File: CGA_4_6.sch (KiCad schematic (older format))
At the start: 11 parts, among them U1 74S112, U2 74LS74, U25 74LS00, U26 74S04, U28 74LS10, U29 74S04, U30 74LS32, U46 74LS00, U47 74LS51, U49 74LS02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

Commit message: More sheet 4
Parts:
- added U27: 74LS51, Package_DIP:DIP-14_W7.62mm_LongPads, symbol 74xx:74LS51
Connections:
- net HRES: now also U27.2
- net ~CCLK: now also U27.6
- net ~HRES: now also U27.4
- new net HCLK: U27.3
- new net LCLK: U27.5
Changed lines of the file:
@@
 Wire Wire Line
 	5500 2200 5800 2200
+$Comp
+L 74xx:74LS51 U27
+U 2 1 62FE2980
+P 2050 6650
+F 0 "U27" H 2050 7175 50  0000 C CNN
+F 1 "74LS51" H 2050 7084 50  0000 C CNN
+F 2 "Package_DIP:DIP-14_W7.62mm_LongPads" H 2050 6650 50  0001 C CNN
+F 3 "http://www.ti.com/lit/ds/symlink/sn74ls51.pdf" H 2050 6650 50  0001 C CNN
+	2    2050 6650
+	1    0    0    -1
+$EndComp
+$Comp
+L 74xx:74LS51 U27
+U 1 1 62FEE44E
+P 2050 7900
+F 0 "U27" H 2050 8425 50  0000 C CNN
+F 1 "74LS51" H 2050 8334 50  0000 C CNN
+F 2 "Package_DIP:DIP-14_W7.62mm_LongPads" H 2050 7900 50  0001 C CNN
+F 3 "http://www.ti.com/lit/ds/symlink/sn74ls51.pdf" H 2050 7900 50  0001 C CNN
+	1    2050 7900
+	1    0    0    -1
+$EndComp
+Wire Wire Line
+	1550 6350 1050 6350
+Text GLabel 1050 6350 0    50   Input ~ 0
+HRES
+Wire Wire Line
+	1550 6550 1050 6550
+Text GLabel 1050 6550 0    50   Input ~ 0
+HCLK
+Wire Wire Line
+	1550 6750 1050 6750
+Text GLabel 1050 6750 0    50   Input ~ 0
+~HRES
+Wire Wire Line
+	1550 6950 1050 6950
+Text GLabel 1050 6950 0    50   Input ~ 0
+LCLK
+Text GLabel 2750 6650 2    50   Output ~ 0
+~CCLK
+Wire Wire Line
+	2750 6650 2550 6650
 $EndSCHEMATC

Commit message: More sheet 4
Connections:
- net HRES: now also U27.9
- net VCC: now also U27.10, U27.13
- net ~HRES: now also U27.12
- net ~7_MHZ: now reaches U27.1
- net ~14_MHZ: now reaches U27.11
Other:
- moved on the sheet: U27A, U27B
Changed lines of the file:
@@
 L 74xx:74LS51 U27
 U 2 1 62FE2980
-P 2050 6650
-F 0 "U27" H 2050 7175 50  0000 C CNN
-F 1 "74LS51" H 2050 7084 50  0000 C CNN
-F 2 "Package_DIP:DIP-14_W7.62mm_LongPads" H 2050 6650 50  0001 C CNN
-F 3 "http://www.ti.com/lit/ds/symlink/sn74ls51.pdf" H 2050 6650 50  0001 C CNN
-	2    2050 6650
+P 2100 6200
+F 0 "U27" H 2100 6725 50  0000 C CNN
+F 1 "74LS51" H 2100 6634 50  0000 C CNN
+F 2 "Package_DIP:DIP-14_W7.62mm_LongPads" H 2100 6200 50  0001 C CNN
+F 3 "http://www.ti.com/lit/ds/symlink/sn74ls51.pdf" H 2100 6200 50  0001 C CNN
+	2    2100 6200
 	1    0    0    -1
 $EndComp
@@
 L 74xx:74LS51 U27
 U 1 1 62FEE44E
-P 2050 7900
-F 0 "U27" H 2050 8425 50  0000 C CNN
-F 1 "74LS51" H 2050 8334 50  0000 C CNN
-F 2 "Package_DIP:DIP-14_W7.62mm_LongPads" H 2050 7900 50  0001 C CNN
-F 3 "http://www.ti.com/lit/ds/symlink/sn74ls51.pdf" H 2050 7900 50  0001 C CNN
-	1    2050 7900
+P 2100 7250
+F 0 "U27" H 2100 6760 50  0000 C CNN
+F 1 "74LS51" H 2100 6851 50  0000 C CNN
+F 2 "Package_DIP:DIP-14_W7.62mm_LongPads" H 2100 7250 50  0001 C CNN
+F 3 "http://www.ti.com/lit/ds/symlink/sn74ls51.pdf" H 2100 7250 50  0001 C CNN
+	1    2100 7250
+	1    0    0    1
+$EndComp
+Wire Wire Line
+	1600 5900 1200 5900
+Text GLabel 1100 5900 0    50   Input ~ 0
+HRES
+Wire Wire Line
+	1600 6100 1100 6100
+Text GLabel 1100 6100 0    50   Input ~ 0
+HCLK
+Wire Wire Line
+	1600 6300 1450 6300
+Text GLabel 1100 6300 0    50   Input ~ 0
+~HRES
+Wire Wire Line
+	1600 6500 1100 6500
+Text GLabel 1100 6500 0    50   Input ~ 0
+LCLK
+Text GLabel 2800 6200 2    50   Output ~ 0
+~CCLK
+Wire Wire Line
+	2800 6200 2600 6200
+Wire Wire Line
+	1600 7150 1200 7150
+Wire Wire Line
+	1200 7150 1200 5900
+Connection ~ 1200 5900
+Wire Wire Line
+	1200 5900 1100 5900
+Text GLabel 1100 6950 0    50   Input ~ 0
+~14_MHZ
+Wire Wire Line
+	1100 6950 1600 6950
+Wire Wire Line
+	1600 7050 1350 7050
+Wire Wire Line
+	1350 7050 1350 7300
+Wire Wire Line
+	1350 7350 1600 7350
+$Comp
+L power:VCC #PWR?
+U 1 1 630E9E72
+P 1100 7200
+F 0 "#PWR?" H 1100 7050 50  0001 C CNN
+F 1 "VCC" H 950 7250 50  0000 C CNN
+F 2 "" H 1100 7200 50  0001 C CNN
+F 3 "" H 1100 7200 50  0001 C CNN
+	1    1100 7200
 	1    0    0    -1
 $EndComp
 Wire Wire Line
-	1550 6350 1050 6350
-Text GLabel 1050 6350 0    50   Input ~ 0
-HRES
+	1100 7200 1100 7300
 Wire Wire Line
-	1550 6550 1050 6550
-Text GLabel 1050 6550 0    50   Input ~ 0
-HCLK
+	1100 7300 1350 7300
+Connection ~ 1350 7300
 Wire Wire Line
-	1550 6750 1050 6750
-Text GLabel 1050 6750 0    50   Input ~ 0
-~HRES
+	1350 7300 1350 7350
 Wire Wire Line
-	1550 6950 1050 6950
-Text GLabel 1050 6950 0    50   Input ~ 0
-LCLK
-Text GLabel 2750 6650 2    50   Output ~ 0
-~CCLK
+	1600 7450 1450 7450
 Wire Wire Line
-	2750 6650 2550 6650
+	1450 7450 1450 6300
+Connection ~ 1450 6300
+Wire Wire Line
+	1450 6300 1100 6300
+Text GLabel 1100 7550 0    50   Input ~ 0
+~7_MHZ
+Wire Wire Line
+	1600 7550 1100 7550
 $EndSCHEMATC

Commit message: More sheet 4
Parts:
- added unit 5 of U26
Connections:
- net DOT_CLOCK: now reaches U27.8
- net DOT_CLOCK: now also U26.11
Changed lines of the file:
@@
 Wire Wire Line
 	1600 7550 1100 7550
+$Comp
+L 74xx:74LS04 U?
+U 5 1 63106999
+P 3300 7250
+AR Path="/60463C57/63106999" Ref="U?"  Part="2"
+AR Path="/60463CC5/63106999" Ref="U26"  Part="5"
+F 0 "U26" H 3250 6950 50  0000 C CNN
+F 1 "74S04" H 3250 7050 50  0000 C CNN
+F 2 "Package_DIP:DIP-14_W7.62mm_LongPads" H 3300 7250 50  0001 C CNN
+F 3 "http://www.ti.com/lit/gpn/sn74LS04" H 3300 7250 50  0001 C CNN
+	5    3300 7250
+	1    0    0    -1
+$EndComp
+Wire Wire Line
+	2600 7250 2700 7250
+Wire Wire Line
+	2700 7250 2700 7700
+Wire Wire Line
+	2700 7700 3150 7700
+Connection ~ 2700 7250
+Wire Wire Line
+	2700 7250 3000 7250
+Text GLabel 3150 7700 2    50   Output ~ 0
+DOT_CLOCK
 $EndSCHEMATC

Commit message: More sheet 4
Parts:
- added unit 4 of U25
- added unit 1 of U25
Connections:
- net at U26.10: now also U25.13
- new net: U25.1, U25.11
- new net: U25.12, U25.3
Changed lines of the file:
@@
 Text GLabel 3150 7700 2    50   Output ~ 0
 DOT_CLOCK
+$Comp
+L 74xx:74LS00 U25
+U 4 1 6312E8E0
+P 4350 6900
+F 0 "U25" H 4350 6600 50  0000 C CNN
+F 1 "74LS00" H 4350 6700 50  0000 C CNN
+F 2 "Package_DIP:DIP-14_W7.62mm_LongPads" H 4350 6900 50  0001 C CNN
+F 3 "http://www.ti.com/lit/gpn/sn74ls00" H 4350 6900 50  0001 C CNN
+	4    4350 6900
+	1    0    0    1
+$EndComp
+$Comp
+L 74xx:74LS00 U25
+U 1 1 631459CB
+P 4350 7550
+F 0 "U25" H 4350 7250 50  0000 C CNN
+F 1 "74LS00" H 4350 7350 50  0000 C CNN
+F 2 "Package_DIP:DIP-14_W7.62mm_LongPads" H 4350 7550 50  0001 C CNN
+F 3 "http://www.ti.com/lit/gpn/sn74ls00" H 4350 7550 50  0001 C CNN
+	1    4350 7550
+	1    0    0    -1
+$EndComp
+Wire Wire Line
+	3600 7250 3800 7250
+Wire Wire Line
+	3800 7250 3800 6800
+Wire Wire Line
+	3800 6800 4050 6800
+Wire Wire Line
+	4650 6900 5000 6900
+Wire Wire Line
+	5000 6900 5000 7200
+Wire Wire Line
+	5000 7200 3900 7200
+Wire Wire Line
+	3900 7200 3900 7450
+Wire Wire Line
+	3900 7450 4050 7450
+Wire Wire Line
+	4650 7550 4900 7550
+Wire Wire Line
+	4900 7550 4900 7100
+Wire Wire Line
+	4900 7100 3900 7100
+Wire Wire Line
+	3900 7100 3900 7000
+Wire Wire Line
+	3900 7000 4050 7000
 $EndSCHEMATC

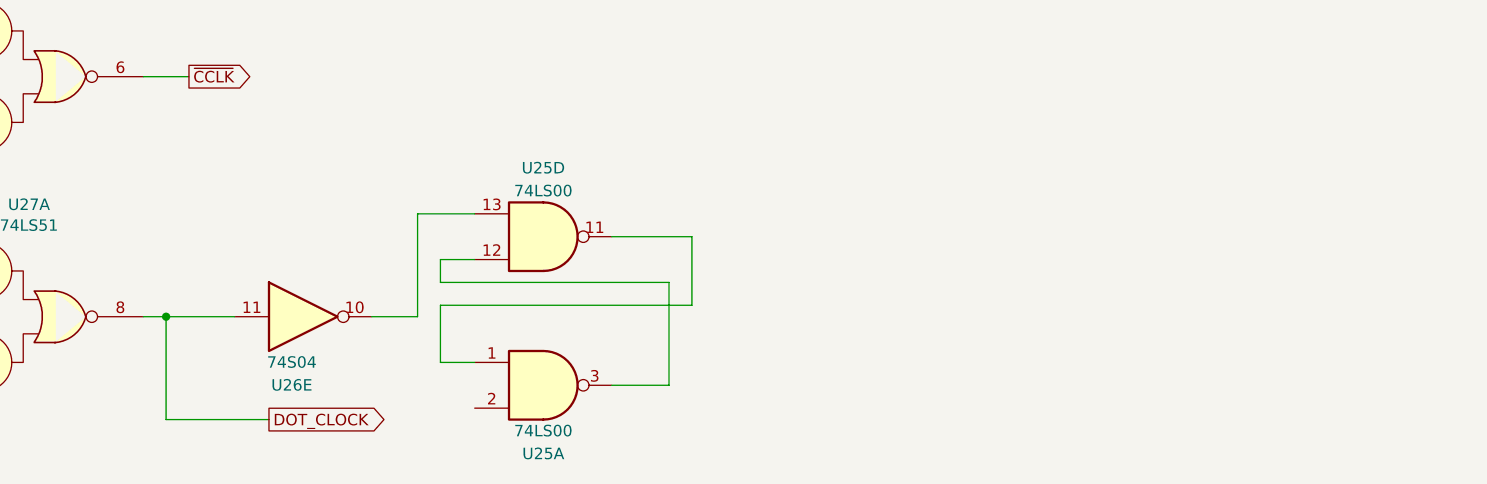
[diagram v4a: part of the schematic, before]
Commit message: Add more of sheet 4
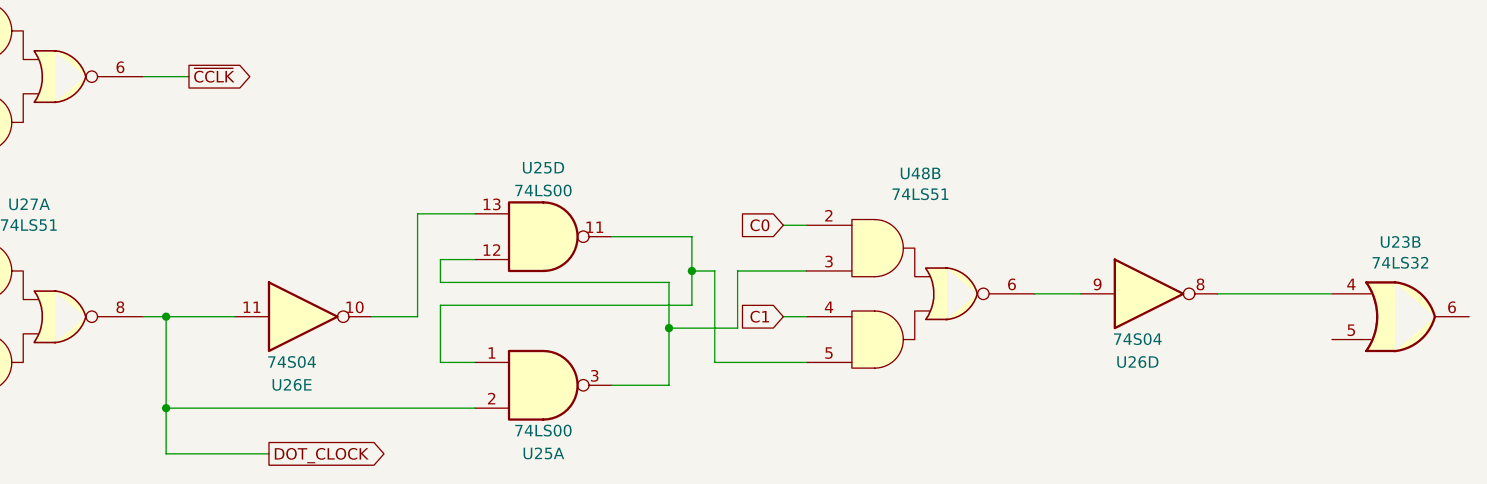
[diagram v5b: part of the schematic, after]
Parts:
- added U23: 74LS32, Package_DIP:DIP-14_W7.62mm_LongPads, symbol 74xx:74LS32
- added unit 4 of U26
- added U48: 74LS51, Package_DIP:DIP-14_W7.62mm_LongPads, symbol 74xx:74LS51
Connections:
- net DOT_CLOCK: now also U25.2
- net at U25.1, U25.11: now also U48.5
- net at U25.12, U25.3: now also U48.3
- new net: U26.9, U48.6
- new net: U23.4, U26.8
- new net C0: U48.2
- new net C1: U48.4
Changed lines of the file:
@@
 	2600 7250 2700 7250
 Wire Wire Line
-	2700 7250 2700 7700
-Wire Wire Line
-	2700 7700 3150 7700
+	2700 7850 3150 7850
 Connection ~ 2700 7250
 Wire Wire Line
 	2700 7250 3000 7250
-Text GLabel 3150 7700 2    50   Output ~ 0
+Text GLabel 3150 7850 2    50   Output ~ 0
 DOT_CLOCK
 $Comp
@@
 	4650 6900 5000 6900
 Wire Wire Line
-	5000 6900 5000 7200
+	5000 6900 5000 7050
 Wire Wire Line
 	5000 7200 3900 7200
@@
 	4650 7550 4900 7550
 Wire Wire Line
-	4900 7550 4900 7100
+	4900 7550 4900 7300
 Wire Wire Line
 	4900 7100 3900 7100
@@
 Wire Wire Line
 	3900 7000 4050 7000
+$Comp
+L 74xx:74LS51 U?
+U 2 1 63173D58
+P 6000 7150
+AR Path="/60463BAE/63173D58" Ref="U?"  Part="1"
+AR Path="/60463CC5/63173D58" Ref="U48"  Part="2"
+F 0 "U48" H 6000 7675 50  0000 C CNN
+F 1 "74LS51" H 6000 7584 50  0000 C CNN
+F 2 "Package_DIP:DIP-14_W7.62mm_LongPads" H 6000 7150 50  0001 C CNN
+F 3 "http://www.ti.com/lit/ds/symlink/sn74ls51.pdf" H 6000 7150 50  0001 C CNN
+	2    6000 7150
+	1    0    0    -1
+$EndComp
+Wire Wire Line
+	4900 7300 5200 7300
+Wire Wire Line
+	5200 7300 5200 7050
+Wire Wire Line
+	5200 7050 5500 7050
+Connection ~ 4900 7300
+Wire Wire Line
+	4900 7300 4900 7100
+Wire Wire Line
+	5000 7050 5100 7050
+Wire Wire Line
+	5100 7050 5100 7450
+Wire Wire Line
+	5100 7450 5500 7450
+Connection ~ 5000 7050
+Wire Wire Line
+	5000 7050 5000 7200
+Text GLabel 5400 7250 0    50   Input ~ 0
+C1
+Wire Wire Line
+	5400 7250 5500 7250
+Text GLabel 5400 6850 0    50   Input ~ 0
+C0
+Wire Wire Line
+	5400 6850 5500 6850
+$Comp
+L 74xx:74LS04 U?
+U 4 1 631E3E02
+P 7000 7150
+AR Path="/60463C57/631E3E02" Ref="U?"  Part="2"
+AR Path="/60463CC5/631E3E02" Ref="U26"  Part="4"
+F 0 "U26" H 6950 6850 50  0000 C CNN
+F 1 "74S04" H 6950 6950 50  0000 C CNN
+F 2 "Package_DIP:DIP-14_W7.62mm_LongPads" H 7000 7150 50  0001 C CNN
+F 3 "http://www.ti.com/lit/gpn/sn74LS04" H 7000 7150 50  0001 C CNN
+	4    7000 7150
+	1    0    0    -1
+$EndComp
+Wire Wire Line
+	6500 7150 6700 7150
+$Comp
+L 74xx:74LS32 U23
+U 2 1 631F965E
+P 8100 7250
+F 0 "U23" H 8100 7575 50  0000 C CNN
+F 1 "74LS32" H 8100 7484 50  0000 C CNN
+F 2 "Package_DIP:DIP-14_W7.62mm_LongPads" H 8100 7250 50  0001 C CNN
+F 3 "http://www.ti.com/lit/gpn/sn74LS32" H 8100 7250 50  0001 C CNN
+	2    8100 7250
+	1    0    0    -1
+$EndComp
+Wire Wire Line
+	7300 7150 7800 7150
+Wire Wire Line
+	2700 7250 2700 7650
+Wire Wire Line
+	4050 7650 2700 7650
+Connection ~ 2700 7650
+Wire Wire Line
+	2700 7650 2700 7850
 $EndSCHEMATC

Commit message: More sheet 4
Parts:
- added U15: 74LS00, Package_DIP:DIP-14_W7.62mm_LongPads, symbol 74xx:74LS00
- added unit 1 of U28
- added U65: 74LS02, Package_DIP:DIP-14_W7.62mm_LongPads, symbol 74xx:74LS02
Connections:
- net at U23.6: now also U28.13
- new net: U15.11, U28.1
- new net: U28.2, U65.4
- new net HSYNC_DLY: U65.6
- new net STR: U28.12
- new net VSYNC_DLY: U65.5
- new net ~DISPEN_DLY: U15.13
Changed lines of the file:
@@
 Wire Wire Line
 	2700 7650 2700 7850
+$Comp
+L 74xx:74LS00 U?
+U 4 1 63236E76
+P 8100 6600
+AR Path="/60463C57/63236E76" Ref="U?"  Part="4"
+AR Path="/60463CC5/63236E76" Ref="U15"  Part="4"
+F 0 "U15" H 8100 6283 50  0000 C CNN
+F 1 "74LS00" H 8100 6374 50  0000 C CNN
+F 2 "Package_DIP:DIP-14_W7.62mm_LongPads" H 8100 6600 50  0001 C CNN
+F 3 "http://www.ti.com/lit/gpn/sn74ls00" H 8100 6600 50  0001 C CNN
+	4    8100 6600
+	1    0    0    1
+$EndComp
+$Comp
+L 74xx:74LS02 U?
+U 2 1 6325627C
+P 8100 6000
+AR Path="/60463C57/6325627C" Ref="U?"  Part="4"
+AR Path="/60463CC5/6325627C" Ref="U65"  Part="2"
+F 0 "U65" H 8100 6325 50  0000 C CNN
+F 1 "74LS02" H 8100 6234 50  0000 C CNN
+F 2 "Package_DIP:DIP-14_W7.62mm_LongPads" H 8100 6000 50  0001 C CNN
+F 3 "http://www.ti.com/lit/gpn/sn74ls02" H 8100 6000 50  0001 C CNN
+	2    8100 6000
+	1    0    0    -1
+$EndComp
+$Comp
+L 74xx:74LS10 U?
+U 1 1 63279063
+P 9050 6700
+AR Path="/60463BAE/63279063" Ref="U?"  Part="3"
+AR Path="/60463CC5/63279063" Ref="U28"  Part="1"
+F 0 "U28" H 9050 7025 50  0000 C CNN
+F 1 "74LS10" H 9050 6934 50  0000 C CNN
+F 2 "Package_DIP:DIP-14_W7.62mm_LongPads" H 9050 6700 50  0001 C CNN
+F 3 "http://www.ti.com/lit/gpn/sn74LS10" H 9050 6700 50  0001 C CNN
+	1    9050 6700
+	1    0    0    -1
+$EndComp
+Wire Wire Line
+	8400 6600 8750 6600
+Wire Wire Line
+	8400 6000 8600 6000
+Wire Wire Line
+	8600 6000 8600 6700
+Wire Wire Line
+	8600 6700 8750 6700
+Wire Wire Line
+	8400 7250 8600 7250
+Wire Wire Line
+	8600 7250 8600 6800
+Wire Wire Line
+	8600 6800 8750 6800
+Text GLabel 9650 6700 2    50   Output ~ 0
+STR
+Wire Wire Line
+	9350 6700 9650 6700
+Text GLabel 7300 5900 0    50   Input ~ 0
+VSYNC_DLY
+Wire Wire Line
+	7300 5900 7800 5900
+Text GLabel 7300 6100 0    50   Input ~ 0
+HSYNC_DLY
+Wire Wire Line
+	7300 6100 7800 6100
+Text GLabel 7300 6500 0    50   Input ~ 0
+~DISPEN_DLY
+Wire Wire Line
+	7300 6500 7800 6500
 $EndSCHEMATC

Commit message: Sheet 4
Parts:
- added unit 1 of U23
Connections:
- net C0: now also U23.2
- net C1: now also U23.1
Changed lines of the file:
@@
 Wire Wire Line
 	7300 6500 7800 6500
+$Comp
+L 74xx:74LS32 U23
+U 1 1 6330493E
+P 1850 8600
+F 0 "U23" H 1850 8925 50  0000 C CNN
+F 1 "74LS32" H 1850 8834 50  0000 C CNN
+F 2 "Package_DIP:DIP-14_W7.62mm_LongPads" H 1850 8600 50  0001 C CNN
+F 3 "http://www.ti.com/lit/gpn/sn74LS32" H 1850 8600 50  0001 C CNN
+	1    1850 8600
+	1    0    0    -1
+$EndComp
+Text GLabel 1150 8500 0    50   Input ~ 0
+C1
+Wire Wire Line
+	1150 8500 1550 8500
+Text GLabel 1150 8700 0    50   Input ~ 0
+C0
+Wire Wire Line
+	1150 8700 1550 8700
 $EndSCHEMATC

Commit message: More sheet 4
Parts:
- added U22: 74LS51, Package_DIP:DIP-14_W7.62mm_LongPads, symbol 74xx:74LS51
- added U40: 74LS174, Package_DIP:DIP-16_W7.62mm_LongPads, symbol 74xx:74LS174
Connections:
- net VCC: now also U22.9, U40.16 (VCC)
- net ~GRPH: now also U22.10
- net at U23.3: now also U22.1
- new net: U22.13, U40.5 (Q1)
- new net ALPHA_DOTS: U22.11
- new net D0: U40.3 (D0)
- new net D1: U40.4 (D1)
- new net D2: U40.6 (D2)
- new net D3: U40.11 (D3)
- new net D4: U40.13 (D4)
- new net D5: U40.14 (D5)
- new net GND: U40.8 (GND)
- new net ~RESET: U40.1 (~Mr)
- new net ~SEL_1: U40.9 (Cp)
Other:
- moved on the sheet: U23A
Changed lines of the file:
@@
 L 74xx:74LS32 U23
 U 1 1 6330493E
-P 1850 8600
-F 0 "U23" H 1850 8925 50  0000 C CNN
-F 1 "74LS32" H 1850 8834 50  0000 C CNN
-F 2 "Package_DIP:DIP-14_W7.62mm_LongPads" H 1850 8600 50  0001 C CNN
-F 3 "http://www.ti.com/lit/gpn/sn74LS32" H 1850 8600 50  0001 C CNN
-	1    1850 8600
+P 2300 8850
+F 0 "U23" H 2300 9175 50  0000 C CNN
+F 1 "74LS32" H 2300 9084 50  0000 C CNN
+F 2 "Package_DIP:DIP-14_W7.62mm_LongPads" H 2300 8850 50  0001 C CNN
+F 3 "http://www.ti.com/lit/gpn/sn74LS32" H 2300 8850 50  0001 C CNN
+	1    2300 8850
 	1    0    0    -1
 $EndComp
-Text GLabel 1150 8500 0    50   Input ~ 0
+Text GLabel 1600 8750 0    50   Input ~ 0
 C1
 Wire Wire Line
-	1150 8500 1550 8500
-Text GLabel 1150 8700 0    50   Input ~ 0
+	1600 8750 2000 8750
+Text GLabel 1600 8950 0    50   Input ~ 0
 C0
 Wire Wire Line
-	1150 8700 1550 8700
+	1600 8950 2000 8950
+$Comp
+L 74xx:74LS51 U22
+U 1 1 6337DF08
+P 3550 8550
+F 0 "U22" H 3550 8060 50  0000 C CNN
+F 1 "74LS51" H 3550 8151 50  0000 C CNN
+F 2 "Package_DIP:DIP-14_W7.62mm_LongPads" H 3550 8550 50  0001 C CNN
+F 3 "http://www.ti.com/lit/ds/symlink/sn74ls51.pdf" H 3550 8550 50  0001 C CNN
+	1    3550 8550
+	1    0    0    1
+$EndComp
+Wire Wire Line
+	2600 8850 3050 8850
+$Comp
+L power:VCC #PWR?
+U 1 1 633C357D
+P 2800 8100
+F 0 "#PWR?" H 2800 7950 50  0001 C CNN
+F 1 "VCC" H 2815 8273 50  0000 C CNN
+F 2 "" H 2800 8100 50  0001 C CNN
+F 3 "" H 2800 8100 50  0001 C CNN
+	1    2800 8100
+	1    0    0    -1
+$EndComp
+Wire Wire Line
+	3050 8450 2800 8450
+Wire Wire Line
+	2800 8450 2800 8100
+Wire Wire Line
+	3050 8350 1600 8350
+Text GLabel 1600 8350 0    50   Input ~ 0
+~GRPH
+Wire Wire Line
+	3050 8250 1600 8250
+Text GLabel 1600 8250 0    50   Input ~ 0
+ALPHA_DOTS
+$Comp
+L 74xx:74LS174 U40
+U 1 1 63419162
+P 2250 10000
+F 0 "U40" H 2000 10550 50  0000 C CNN
+F 1 "74LS174" H 2500 10550 50  0000 C CNN
+F 2 "Package_DIP:DIP-16_W7.62mm_LongPads" H 2250 10000 50  0001 C CNN
+F 3 "http://www.ti.com/lit/gpn/sn74LS174" H 2250 10000 50  0001 C CNN
+	1    2250 10000
+	1    0    0    -1
+$EndComp
+$Comp
+L power:VCC #PWR?
+U 1 1 6341CA1D
+P 2250 9300
+F 0 "#PWR?" H 2250 9150 50  0001 C CNN
+F 1 "VCC" H 2265 9473 50  0000 C CNN
+F 2 "" H 2250 9300 50  0001 C CNN
+F 3 "" H 2250 9300 50  0001 C CNN
+	1    2250 9300
+	1    0    0    -1
+$EndComp
+$Comp
+L power:GND #PWR?
+U 1 1 6341DF93
+P 2250 10800
+F 0 "#PWR?" H 2250 10550 50  0001 C CNN
+F 1 "GND" H 2255 10627 50  0000 C CNN
+F 2 "" H 2250 10800 50  0001 C CNN
+F 3 "" H 2250 10800 50  0001 C CNN
+	1    2250 10800
+	1    0    0    -1
+$EndComp
+Text GLabel 1050 10300 0    50   Input ~ 0
+~SEL_1
+Wire Wire Line
+	1050 10300 1750 10300
+Text GLabel 1050 10500 0    50   Input ~ 0
+~RESET
+Wire Wire Line
+	1050 10500 1750 10500
+Wire Wire Line
+	1750 9600 1050 9600
+Wire Wire Line
+	1750 9700 1050 9700
+Wire Wire Line
+	1750 9800 1050 9800
+Wire Wire Line
+	1750 9900 1050 9900
+Wire Wire Line
+	1750 10000 1050 10000
+Wire Wire Line
+	1750 10100 1050 10100
+Text GLabel 1050 9600 0    50   Input ~ 0
+D0
+Text GLabel 1050 9700 0    50   Input ~ 0
+D1
+Text GLabel 1050 9800 0    50   Input ~ 0
+D2
+Text GLabel 1050 9900 0    50   Input ~ 0
+D3
+Text GLabel 1050 10000 0    50   Input ~ 0
+D4
+Text GLabel 1050 10100 0    50   Input ~ 0
+D5
+Wire Wire Line
+	3050 8650 2900 8650
+Wire Wire Line
+	2900 8650 2900 9700
+Wire Wire Line
+	2900 9700 2750 9700
 $EndSCHEMATC
